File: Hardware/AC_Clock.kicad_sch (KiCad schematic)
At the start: 56 parts, among them J1 L, J2 N, J5 Minutes, J6 Hours, SW1 Min_PB, SW2 Hr_PB, SW3 Hour Set, SW4 Min Set, T1 10:1, U1 AZ1117-5.0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

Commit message: Remove old ICs
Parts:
- removed C4, C5: 0.1u, Capacitor_SMD:C_0603_1608Metric, symbol Device:C_Small
- removed D10, D11, D12, D13, D14, D15, D16, D17, D18, D19, D6, D7, D8, D9: 1N4148WT, Diode_SMD:D_SOD-523, symbol Diode:1N4148WT
- removed JP1: Freq Sel., Jumper:SolderJumper-3_P1.3mm_Bridged12_RoundedPad1.0x1.5mm, symbol Jumper:Jumper_3_Bridged12
- removed R10, R4, R5, R6, R7, R8, R9: 1k, Resistor_SMD:R_0603_1608Metric, symbol Device:R
- removed SW1: Min_PB, Button_Switch_SMD:SW_SPST_PTS645, symbol Switch:SW_Push
- removed SW2: Hr_PB, Button_Switch_SMD:SW_SPST_PTS645, symbol Switch:SW_Push
- removed U4, U5: 74LS393, Package_DIP:DIP-14_W7.62mm, symbol 74xx:74LS393
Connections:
- net 10hr: now also U15.7 (CO), U16.3 (C)
- net hour: now also SW3.1 (A), U14.7 (Reset), U17.11
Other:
- note removed: "Change to CD4510 & J/K Flip flop HEF4027 ?"
- note removed: "Change to? CD4518"
- note removed: "Count Hours"
- note removed: "Count Minutes"
- note removed: "Set Time"

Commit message: Change transformers and clean up some wiring
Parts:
- T1: value 10:1 -> F12-500-C2; footprint JKC_Library:Transformer_CL2-5.0R-12 -> JKC_Library:XFMR_Triad_F12-500-C2; symbol JKC_library:CL2-x -> JKC_library:XFMR_Triad_F12-500-C2; MANUFACTURER (none) -> Triad Magnetics
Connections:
- net AC_12+: now also T1.5; no longer T1.12
- net AC_12-: now also T1.8; no longer T1.7
- net Earth: no longer T1.1
- net Fused: now also T1.1; no longer T1.3, T1.6
- new net: T1.6, T1.7
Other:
- moved on the sheet: C10

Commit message: Clean up wiring and add comments
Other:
- note added: "-> 60Hz count"
- note added: "Hr 1's Rising edge"
- note added: "Min 1's Falling edge"
- note added: "Min 10's Falling edge"
- note added: "Optocoupler"
- note removed: "Optocoupler -> 60Hz count"
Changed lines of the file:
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@@
 	(wire
 		(pts
-			(xy 231.14 99.06) (xy 231.14 69.85)
+			(xy 236.22 99.06) (xy 236.22 69.85)
 		)
 		(stroke
@@
 	(wire
 		(pts
-			(xy 231.14 69.85) (xy 248.92 69.85)
+			(xy 236.22 69.85) (xy 248.92 69.85)
 		)
 		(stroke
@@
 	(wire
 		(pts
-			(xy 220.98 99.06) (xy 231.14 99.06)
+			(xy 220.98 99.06) (xy 236.22 99.06)
 		)
 		(stroke
@@
 		)
 	)
+	(text "-> 60Hz count"
+		(exclude_from_sim no)
+		(at 176.53 38.608 0)
+		(effects
+			(font
+				(size 1.27 1.27)
+			)
+		)
+	)
 	(text "30 Hz"
 		(exclude_from_sim no)
@@
 		)
 	)
-	(text "Optocoupler \n-> 60Hz count"
+	(text "Optocoupler"
 		(exclude_from_sim no)
-		(at 164.084 19.812 0)
+		(at 159.004 18.542 0)
 		(effects
 			(font
@@
 		)
 	)
+	(text "Min 10's\nFalling edge"
+		(exclude_from_sim no)
+		(at 229.87 82.804 0)
+		(effects
+			(font
+				(size 1.27 1.27)
+			)
+		)
+	)
 	(text "AC In"
 		(exclude_from_sim no)
@@
 		)
 	)
+	(text "Min 1's\nFalling edge"
+		(exclude_from_sim no)
+		(at 259.334 83.058 0)
+		(effects
+			(font
+				(size 1.27 1.27)
+			)
+		)
+	)
 	(text "2.1333 s"
 		(exclude_from_sim no)
@@
 		)
 	)
+	(text "Hr 1's\nRising edge"
+		(exclude_from_sim no)
+		(at 188.214 73.152 0)
+		(effects
+			(font
+				(size 1.27 1.27)
+			)
+		)
+	)
 	(label "Pulse"
 		(at 27.94 76.2 0)
@@
 	)
 	(label "10m"
-		(at 231.14 69.85 0)
+		(at 236.22 69.85 0)
 		(fields_autoplaced yes)
 		(effects
@@
 		(dnp no)
 		(property "Reference" "SW3"
-			(at 191.516 107.696 0)
+			(at 191.77 109.474 0)
 			(effects
 				(font
@@
 		)
 		(property "Value" "Hour Set"
-			(at 189.738 109.728 0)
+			(at 198.12 119.126 0)
 			(effects
 				(font

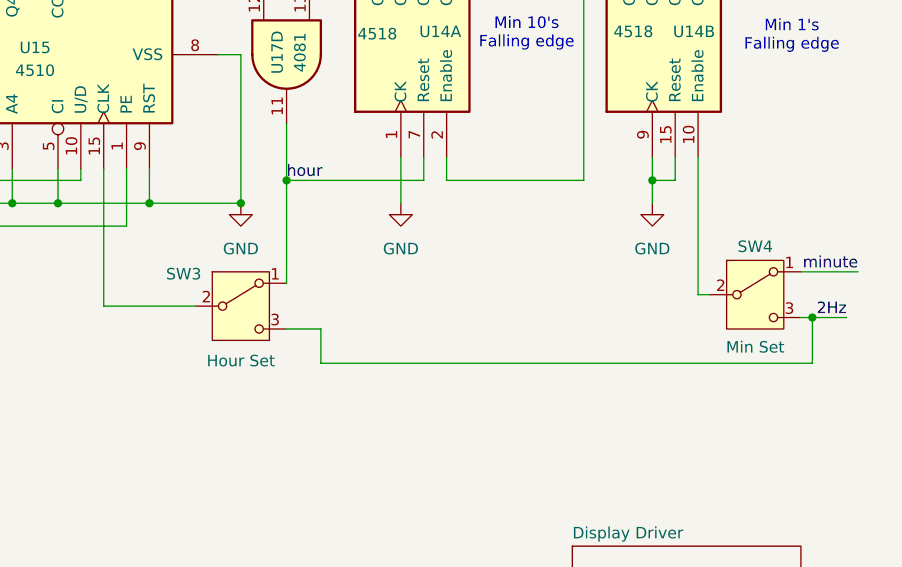
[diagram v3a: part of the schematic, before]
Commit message: Update component symbols and footpints
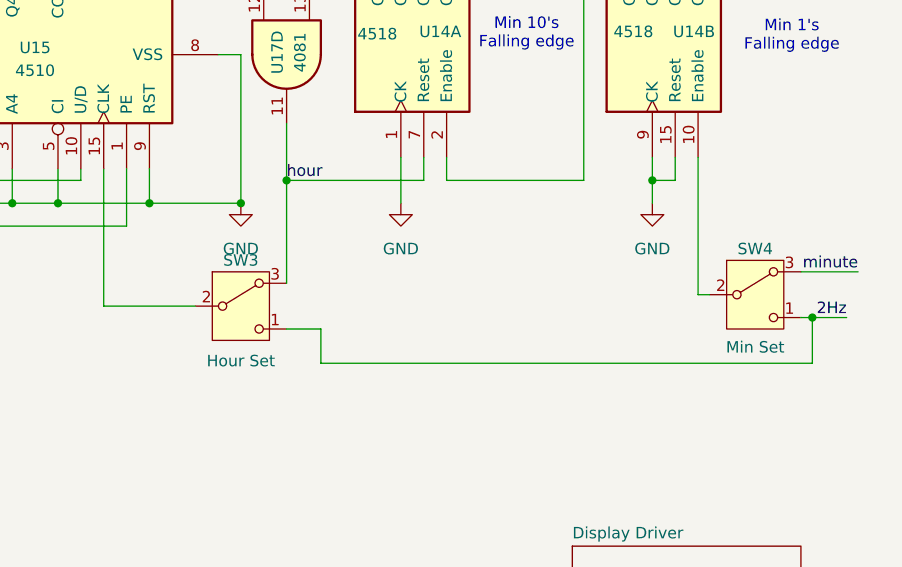
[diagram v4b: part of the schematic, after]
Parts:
- C10: footprint (none) -> Capacitor_THT:C_Disc_D10.5mm_W5.0mm_P7.50mm
- SW3, SW4: footprint (none) -> JKC_Library:SW_Push_CK_PN11SBNA03QE_SPDT_Right_Angle; symbol Switch:SW_SPDT -> Switch:SW_SPDT_321; MPN (none) -> PN11SBNA03QE
- U14, U15, U16: footprint (none) -> Package_DIP:DIP-16_W7.62mm
- U17: footprint (none) -> Package_DIP:DIP-14_W7.62mm
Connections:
- net 2Hz: now also SW3.1 (C), SW4.1 (C); no longer SW3.3 (C), SW4.3 (C)
- net hour: now also SW3.3 (A); no longer SW3.1 (A)
- net minute: now also SW4.3 (A); no longer SW4.1 (A)
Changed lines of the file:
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@@
 			)
 		)
-		(property "Footprint" ""
+		(property "Footprint" "Package_DIP:DIP-14_W7.62mm"
 			(at 203.2 85.09 0)
 			(effects
@@
 			)
 		)
-		(property "Footprint" ""
+		(property "Footprint" "Package_DIP:DIP-16_W7.62mm"
 			(at 228.6 35.56 0)
 			(effects
@@
 			)
 		)
-		(property "Footprint" ""
+		(property "Footprint" "Package_DIP:DIP-16_W7.62mm"
 			(at 175.26 85.09 0)
 			(effects
@@
 			)
 		)
-		(property "Footprint" ""
+		(property "Footprint" "Package_DIP:DIP-14_W7.62mm"
 			(at 241.3 35.56 0)
 			(effects
@@
 			)
 		)
-		(property "Footprint" ""
+		(property "Footprint" "Package_DIP:DIP-14_W7.62mm"
 			(at 132.08 114.3 0)
 			(effects
@@
 			)
 		)
-		(property "Footprint" ""
+		(property "Footprint" "Package_DIP:DIP-14_W7.62mm"
 			(at 135.89 64.77 0)
 			(effects
@@
 			)
 		)
-		(property "Footprint" ""
+		(property "Footprint" "Package_DIP:DIP-16_W7.62mm"
 			(at 142.24 90.17 0)
 			(effects
@@
 			)
 		)
-		(property "Footprint" ""
+		(property "Footprint" "Package_DIP:DIP-16_W7.62mm"
 			(at 215.9 83.82 0)
 			(effects
@@
 			)
 		)
-		(property "Footprint" ""
+		(property "Footprint" "Package_DIP:DIP-14_W7.62mm"
 			(at 128.27 96.52 0)
 			(effects
@@
 			)
 		)
-		(property "Footprint" ""
+		(property "Footprint" "Package_DIP:DIP-16_W7.62mm"
 			(at 116.84 64.77 0)
 			(effects
@@
 	)
 	(symbol
-		(lib_id "Switch:SW_SPDT")
+		(lib_id "Switch:SW_SPDT_321")
 		(at 198.12 113.03 0)
 		(unit 1)
@@
 		(dnp no)
 		(property "Reference" "SW3"
-			(at 191.77 109.474 0)
+			(at 198.12 107.95 0)
 			(effects
 				(font
@@
 			)
 		)
-		(property "Footprint" ""
+		(property "Footprint" "JKC_Library:SW_Push_CK_PN11SBNA03QE_SPDT_Right_Angle"
 			(at 198.12 113.03 0)
 			(effects
@@
 			)
 		)
+		(property "MPN" "PN11SBNA03QE"
+			(at 198.12 113.03 0)
+			(effects
+				(font
+					(size 1.27 1.27)
+				)
+				(hide yes)
+			)
+		)
 		(pin "2"
 		)
@@
 	)
 	(symbol
-		(lib_id "Switch:SW_SPDT")
+		(lib_id "Switch:SW_SPDT_321")
 		(at 255.27 111.76 0)
 		(unit 1)
@@
 		(dnp no)
 		(property "Reference" "SW4"
-			(at 255.27 106.426 0)
+			(at 255.27 106.68 0)
 			(effects
 				(font
@@
 			)
 		)
-		(property "Footprint" ""
+		(property "Footprint" "JKC_Library:SW_Push_CK_PN11SBNA03QE_SPDT_Right_Angle"
 			(at 255.27 111.76 0)
 			(effects
@@
 			)
 		)
+		(property "MPN" "PN11SBNA03QE"
+			(at 255.27 111.76 0)
+			(effects
+				(font
+					(size 1.27 1.27)
+				)
+				(hide yes)
+			)
+		)
 		(pin "2"
 		)
@@
 			)
 		)
-		(property "Footprint" ""
+		(property "Footprint" "Capacitor_THT:C_Disc_D10.5mm_W5.0mm_P7.50mm"
 			(at 59.69 44.45 0)
 			(effects
@@
 			)
 		)
-		(property "Footprint" ""
+		(property "Footprint" "Package_DIP:DIP-16_W7.62mm"
 			(at 243.84 83.82 0)
 			(effects
@@
 			)
 		)
-		(property "Footprint" ""
+		(property "Footprint" "Package_DIP:DIP-16_W7.62mm"
 			(at 215.9 35.56 0)
 			(effects

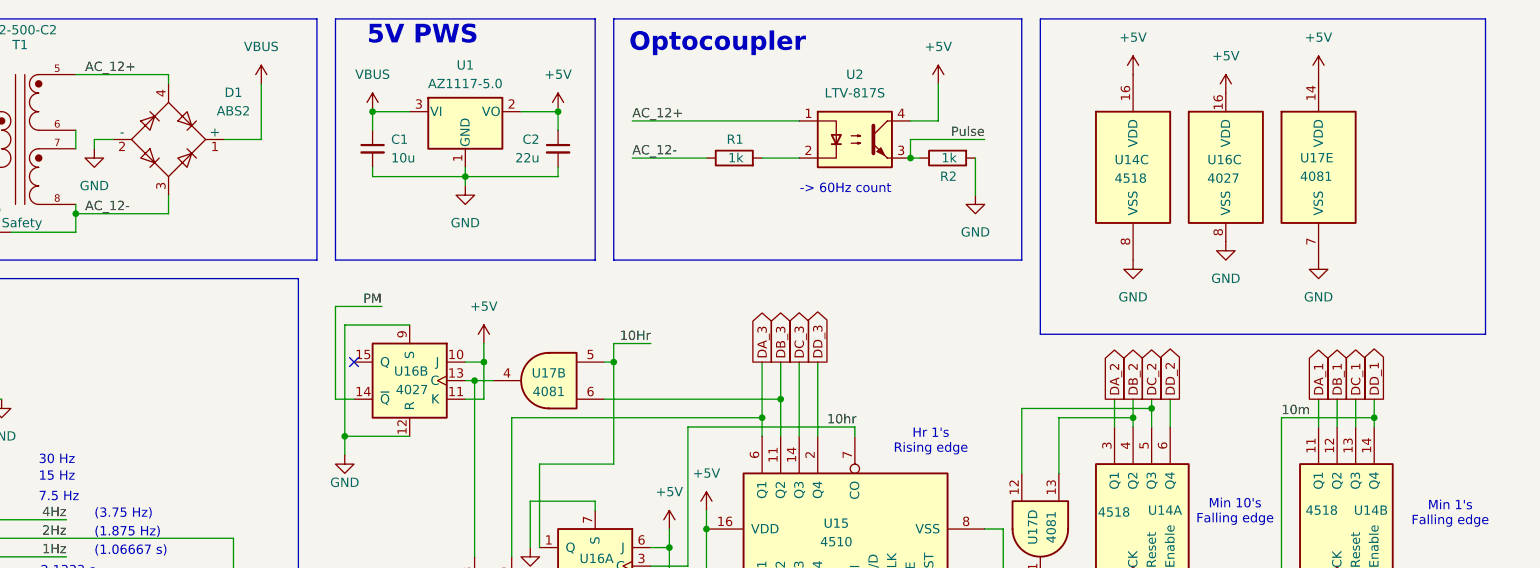
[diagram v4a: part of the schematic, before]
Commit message: Convert layout to 3 board design (power/logic/display)
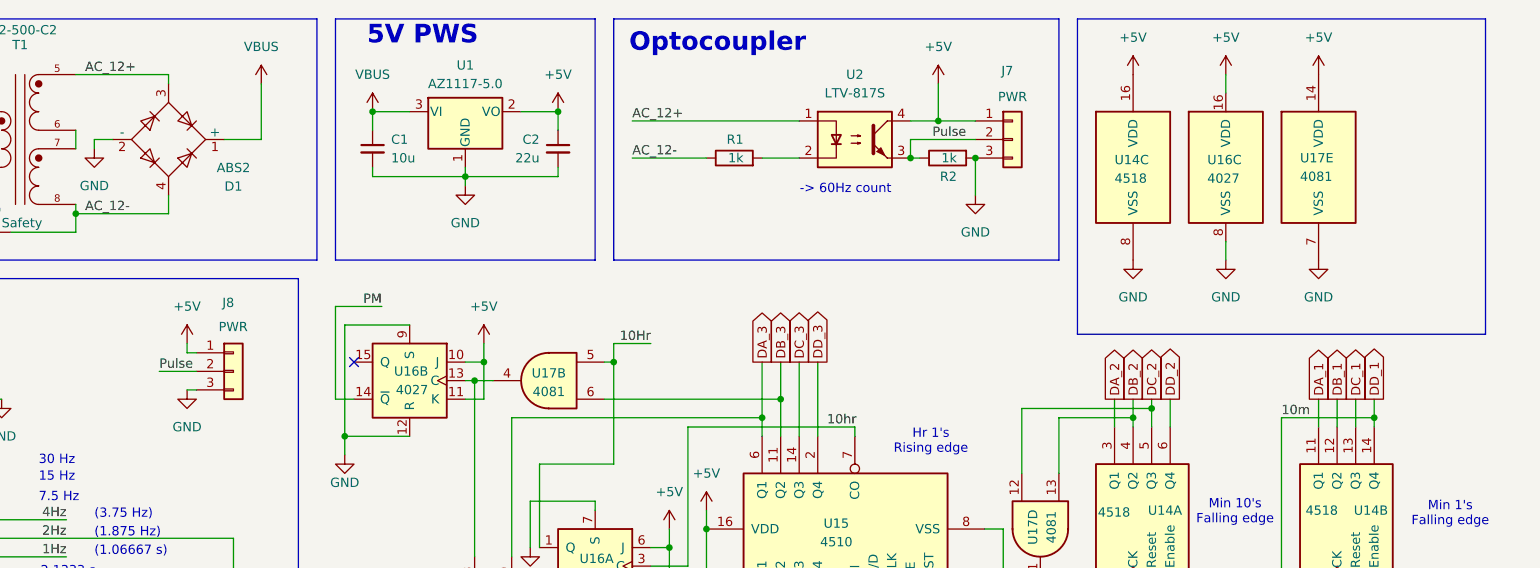
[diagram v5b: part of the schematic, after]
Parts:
- added J7: PWR, Connector_PinSocket_2.54mm:PinSocket_1x03_P2.54mm_Vertical, symbol Connector_Generic:Conn_01x03
- added J8: PWR, Connector_PinHeader_2.54mm:PinHeader_1x03_P2.54mm_Vertical, symbol Connector_Generic:Conn_01x03
- J5, J6: footprint Connector_PinHeader_2.54mm:PinHeader_1x10_P2.54mm_Vertical -> Connector_PinHeader_2.54mm:PinHeader_1x10_P2.54mm_Horizontal
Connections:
- net +5V: now also J7.1 (Pin_1), J8.1 (Pin_1)
- net AC_12+: now also D1.3; no longer D1.4
- net AC_12-: now also D1.4; no longer D1.3
- net GND: now also J7.3 (Pin_3), J8.3 (Pin_3)
- net Pulse: now also J7.2 (Pin_2), J8.2 (Pin_2)

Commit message: Route traces on new layout
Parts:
- removed U14: 4518, Package_DIP:DIP-16_W7.62mm, symbol 4xxx:4518
- added U4: 4518, Package_DIP:DIP-16_W7.62mm, symbol 4xxx:4518
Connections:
- net +5V: now also U4.16 (VDD)
- net DA_1: now also U4.3 (Q1)
- net DA_2: now also U4.11 (Q1)
- net DB_1: now also U4.4 (Q2)
- net DB_2: now also U4.12 (Q2)
- net DC_1: now also U4.5 (Q3)
- net DC_2: now also U4.13 (Q3)
- net DD_1: now also U4.10 (Enable), U4.6 (Q4)
- net DD_2: now also U4.14 (Q4)
- net GND: now also U4.1 (CK), U4.7 (Reset), U4.8 (VSS), U4.9 (CK)
- net hour: now also U4.15 (Reset)
- net hr: now reaches SW3.2 (B), U15.15 (CLK)
- net min: now reaches SW4.2 (B)
- net min: now also U4.2 (Enable)

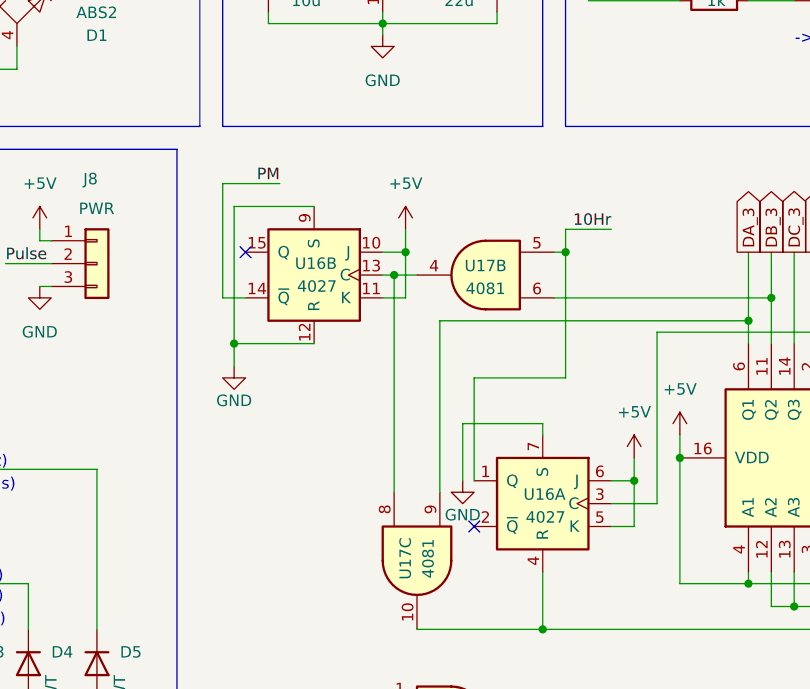
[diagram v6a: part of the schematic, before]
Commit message: Update board layout to minimize space used
Signed-off-by: Joel Cranmer <42.joel.cranmer@gmail.com>
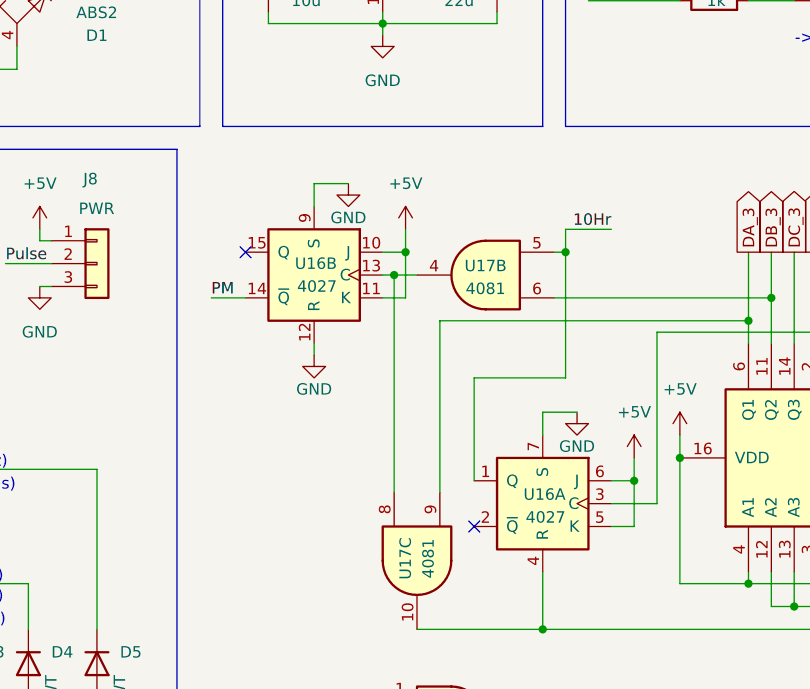
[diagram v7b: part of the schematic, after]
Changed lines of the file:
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@@
 	)
 	(junction
-		(at 107.95 72.39)
-		(diameter 0)
-		(color 0 0 0 0)
-	)
-	(junction
 		(at 124.46 36.83)
 		(diameter 0)
@@
 	(wire
 		(pts
-			(xy 107.95 57.15) (xy 107.95 72.39)
-		)
-		(stroke
-			(width 0)
-			(type default)
-		)
-	)
-	(wire
-		(pts
 			(xy 172.72 101.6) (xy 177.8 101.6)
 		)
@@
 	(wire
 		(pts
-			(xy 133.35 87.63) (xy 133.35 81.28)
-		)
-		(stroke
-			(width 0)
-			(type default)
-		)
-	)
-	(wire
-		(pts
 			(xy 134.62 76.2) (xy 144.78 76.2)
 		)
@@
 	(wire
 		(pts
-			(xy 133.35 81.28) (xy 142.24 81.28)
+			(xy 146.05 80.01) (xy 142.24 80.01)
 		)
 		(stroke
@@
 	(wire
 		(pts
-			(xy 116.84 57.15) (xy 107.95 57.15)
-		)
-		(stroke
-			(width 0)
-			(type default)
-		)
-	)
-	(wire
-		(pts
 			(xy 132.08 27.94) (xy 137.16 27.94)
 		)
@@
 	(wire
 		(pts
-			(xy 142.24 81.28) (xy 142.24 82.55)
+			(xy 142.24 80.01) (xy 142.24 82.55)
 		)
 		(stroke
@@
 	(wire
 		(pts
+			(xy 116.84 54.61) (xy 120.65 54.61)
+		)
+		(stroke
+			(width 0)
+			(type default)
+		)
+	)
+	(wire
+		(pts
 			(xy 62.23 44.45) (xy 71.12 44.45)
 		)
@@
 	(wire
 		(pts
+			(xy 116.84 57.15) (xy 116.84 54.61)
+		)
+		(stroke
+			(width 0)
+			(type default)
+		)
+	)
+	(wire
+		(pts
 			(xy 130.81 88.9) (xy 130.81 69.85)
 		)
@@
 	(wire
 		(pts
-			(xy 107.95 72.39) (xy 116.84 72.39)
-		)
-		(stroke
-			(width 0)
-			(type default)
-		)
-	)
-	(wire
-		(pts
 			(xy 45.72 36.83) (xy 53.34 36.83)
 		)
@@
 	(wire
 		(pts
-			(xy 106.68 54.61) (xy 113.03 54.61)
-		)
-		(stroke
-			(width 0)
-			(type default)
-		)
-	)
-	(wire
-		(pts
 			(xy 92.71 86.36) (xy 92.71 104.14)
 		)
@@
 	(wire
 		(pts
-			(xy 109.22 67.31) (xy 106.68 67.31)
+			(xy 109.22 67.31) (xy 105.41 67.31)
 		)
 		(stroke
@@
 	(wire
 		(pts
-			(xy 106.68 67.31) (xy 106.68 54.61)
-		)
-		(stroke
-			(width 0)
-			(type default)
-		)
-	)
-	(wire
-		(pts
 			(xy 71.12 41.91) (xy 83.82 41.91)
 		)
@@
 	(wire
 		(pts
-			(xy 107.95 72.39) (xy 107.95 74.93)
+			(xy 116.84 72.39) (xy 116.84 73.66)
 		)
 		(stroke
@@
 	)
 	(label "PM"
-		(at 113.03 54.61 180)
+		(at 105.41 67.31 0)
 		(fields_autoplaced yes)
 		(effects
@@
 				(size 1.27 1.27)
 			)
-			(justify right bottom)
+			(justify left bottom)
 		)
 	)
@@
 	(symbol
 		(lib_id "power:GND")
-		(at 107.95 74.93 0)
+		(at 116.84 73.66 0)
 		(unit 1)
 		(exclude_from_sim no)
@@
 		(dnp no)
 		(property "Reference" "#PWR071"
-			(at 107.95 81.28 0)
+			(at 116.84 80.01 0)
 			(effects
 				(font
@@
 		)
 		(property "Value" "GND"
-			(at 107.95 78.74 0)
+			(at 116.84 77.47 0)
 			(effects
 				(font
@@
 		)
 		(property "Footprint" ""
-			(at 107.95 74.93 0)
+			(at 116.84 73.66 0)
 			(effects
 				(font
@@
 		)
 		(property "Datasheet" ""
-			(at 107.95 74.93 0)
+			(at 116.84 73.66 0)
 			(effects
 				(font
@@
 		)
 		(property "Description" "Power symbol creates a global label with name \"GND\" , ground"
-			(at 107.95 74.93 0)
+			(at 116.84 73.66 0)
 			(effects
 				(font
@@
 	(symbol
 		(lib_id "power:GND")
-		(at 133.35 87.63 0)
+		(at 146.05 80.01 0)
 		(unit 1)
 		(exclude_from_sim no)
@@
 		(dnp no)
 		(property "Reference" "#PWR063"
-			(at 133.35 93.98 0)
+			(at 146.05 86.36 0)
 			(effects
 				(font
@@
 		)
 		(property "Value" "GND"
-			(at 133.35 91.44 0)
+			(at 146.05 83.82 0)
 			(effects
 				(font
@@
 		)
 		(property "Footprint" ""
-			(at 133.35 87.63 0)
+			(at 146.05 80.01 0)
 			(effects
 				(font
@@
 		)
 		(property "Datasheet" ""
-			(at 133.35 87.63 0)
+			(at 146.05 80.01 0)
 			(effects
 				(font
@@
 		)
 		(property "Description" "Power symbol creates a global label with name \"GND\" , ground"
-			(at 133.35 87.63 0)
+			(at 146.05 80.01 0)
 			(effects
 				(font
@@
 					(unit 1)
 				)
+			)
+		)
+	)
+	(symbol
+		(lib_id "power:GND")
+		(at 120.65 54.61 0)
+		(unit 1)
+		(exclude_from_sim no)
+		(in_bom yes)
+		(on_board yes)
+		(dnp no)
+		(property "Reference" "#PWR015"
+			(at 120.65 60.96 0)
+			(effects
+				(font
+					(size 1.27 1.27)
+				)
+				(hide yes)
+			)
+		)
+		(property "Value" "GND"
+			(at 120.65 58.42 0)
+			(effects
+				(font
+					(size 1.27 1.27)
+				)
+			)
+		)
+		(property "Footprint" ""
+			(at 120.65 54.61 0)
+			(effects
+				(font
+					(size 1.27 1.27)
+				)
+				(hide yes)
+			)
+		)
+		(property "Datasheet" ""
+			(at 120.65 54.61 0)
+			(effects
+				(font
+					(size 1.27 1.27)
+				)
+				(hide yes)
+			)
+		)
+		(property "Description" "Power symbol creates a global label with name \"GND\" , ground"
+			(at 120.65 54.61 0)
+			(effects
+				(font
+					(size 1.27 1.27)
+				)
+				(hide yes)
+			)
+		)
+		(pin "1"
+		)
+		(instances
+			(project "AC_Clock"
+				(path "/25ded3d7-7fc5-4a73-82e8-c02ba32fe53a"
+					(reference "#PWR015")
+					(unit 1)
+				)
